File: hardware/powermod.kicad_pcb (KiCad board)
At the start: 4 copper layers, 65 x 40 mm, 77 parts, among them J1 USB_C_IN, J2 USB_C_OUT, J3 JST_PH_2, J4 STEMMA_QT, J5 SWD_HDR, Q1 AON7407, Q2 AON7407, Q3 BSS138, SW1 BUTTON, U1 BM8563, U2 PY32F003F18P6, U3 TPS63020DSJR, U4 TP4056, U5 XC6206P332MR, Y1 32.768kHz

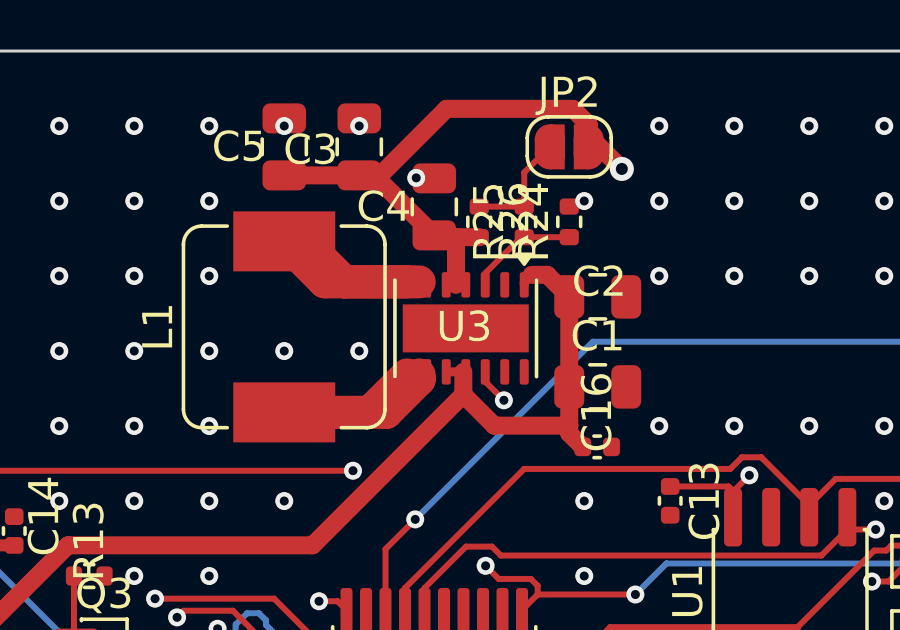
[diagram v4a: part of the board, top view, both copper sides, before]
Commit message: hardware: restore U3 EP plane-tie vias + silk-free gerbers
Validating user's U3 route tweaks (DRC 0, pad-diff 0, VOUT widened to 0.6mm)
surfaced that U3's exposed pad (TPS63020 PGND) had lost its plane-tie/thermal
vias in the re-routes - 0 vias in-pad, nearest GND via 3.6mm. Added 3 tented
GND vias in the EP (drill-safe spacing), DRC still 0. U4 EP already had 1.

Gerbers regenerated WITHOUT F.SilkS/B.SilkS -> fabricated board has no
silkscreen (removes the 127 cosmetic silk warnings from the fab output). Board
file keeps silk for reference; reversible.

Co-Authored-By: Claude Opus 4.8 <noreply@anthropic.com>
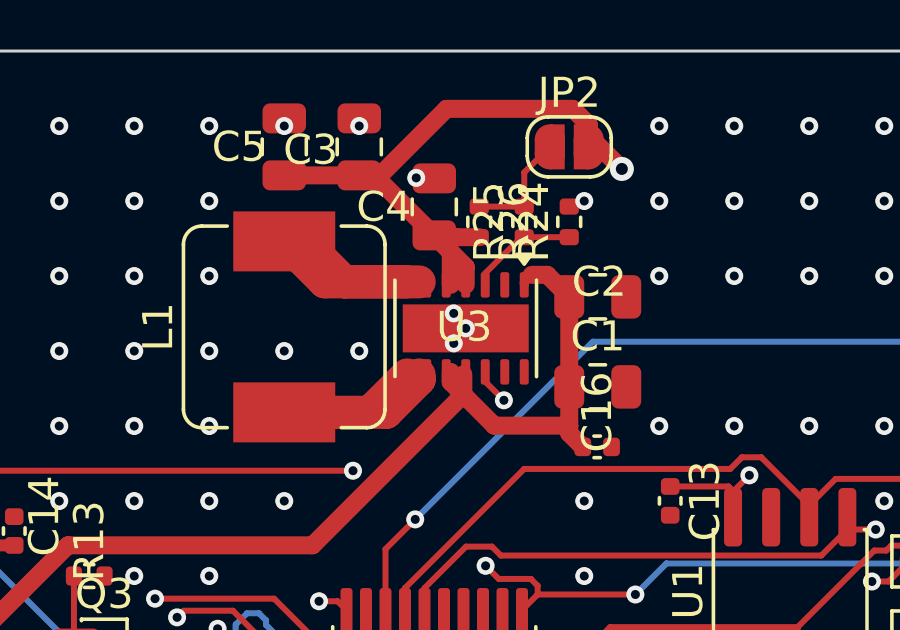
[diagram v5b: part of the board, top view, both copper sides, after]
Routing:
- net VOUT: track 75.1 -> 76.8 mm
- net GND: vias 157 -> 160
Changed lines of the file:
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@@
+	)
+	(via
+		(at 38.15 8.744999)
+		(size 0.6)
+		(drill 0.3)
+		(layers "F.Cu" "B.Cu")
+		(tenting
+			(front yes)
+			(back yes)
+		)
+		(net "GND")
 	)
 	(via
@@
 	)
 	(via
+		(at 38.55 9.245)
+		(size 0.6)
+		(drill 0.3)
+		(layers "F.Cu" "B.Cu")
+		(tenting
+			(front yes)
+			(back yes)
+		)
+		(net "GND")
+	)
+	(via
 		(at 52.5 5)
 		(size 0.6)
@@
 		(drill 0.3)
 		(layers "F.Cu" "B.Cu")
+		(net "GND")
+	)
+	(via
+		(at 38.15 9.744999)
+		(size 0.6)
+		(drill 0.3)
+		(layers "F.Cu" "B.Cu")
+		(tenting
+			(front yes)
+			(back yes)
+		)
 		(net "GND")
 	)
@@
 	)
 	(segment
+		(start 38.4687 11.4533)
+		(end 38.4687 10.7763)
+		(width 0.6)
+		(layer "F.Cu")
+		(net "VSYS")
+	)
+	(segment
 		(start 18.3998 24.3498)
 		(end 18.4 24.35)
@@
 		(start 18.7967 29.3967)
 		(end 19.7948 29.3967)
-		(width 0.6)
-		(layer "F.Cu")
-		(net "VSYS")
-	)
-	(segment
-		(start 37.9 10.695)
-		(end 38.4687 10.695)
-		(width 0.3004)
-		(layer "F.Cu")
-		(net "VSYS")
-	)
-	(segment
-		(start 38.4687 10.695)
-		(end 38.4687 11.4533)
 		(width 0.6)
 		(layer "F.Cu")
@@
 	)
 	(segment
+		(start 38.4687 11.4533)
+		(end 38.0498 11.0344)
+		(width 0.6)
+		(layer "F.Cu")
+		(net "VSYS")
+	)
+	(segment
 		(start 18.4 24.35)
 		(end 18.4 25)
@@
 	)
 	(segment
-		(start 38.4687 10.695)
-		(end 38.55 10.695)
-		(width 0.3004)
-		(layer "F.Cu")
-		(net "VSYS")
-	)
-	(segment
 		(start 27.275 28)
 		(end 27.4375 27.8375)
@@
 		(start 40.75 7.4602)
 		(end 41.2652 7.4602)
+		(width 0.6)
+		(layer "F.Cu")
+		(net "VSYS")
+	)
+	(segment
+		(start 38.0498 11.0344)
+		(end 38.0498 10.695)
 		(width 0.6)
 		(layer "F.Cu")
@@
 	)
 	(segment
+		(start 38.55 7.195)
+		(end 38.55 7.795)
+		(width 0.6)
+		(layer "F.Cu")
+		(net "VOUT")
+	)
+	(segment
 		(start 47.259332 27.0089)
 		(end 48.6093 27.0089)
@@
 	)
 	(segment
+		(start 38.0498 6.6948)
+		(end 38.0498 7.795)
+		(width 0.6)
+		(layer "F.Cu")
+		(net "VOUT")
+	)
+	(segment
 		(start 42.1183 1.9279)
 		(end 42.65 2.4596)
@@
 	)
 	(segment
-		(start 38.225 7.795)
-		(end 37.9 7.795)
-		(width 0.3004)
-		(layer "F.Cu")
-		(net "VOUT")
-	)
-	(segment
 		(start 51.7301 27.0089)
 		(end 52.52 27.7988)
@@
 	)
 	(segment
-		(start 38.55 7.795)
-		(end 38.225 7.795)
-		(width 0.3004)
-		(layer "F.Cu")
-		(net "VOUT")
-	)
-	(segment
 		(start 37.56 6.205)
 		(end 37.5 6.145)
@@
 	)
 	(segment
+		(start 37.5 6.145)
+		(end 38.55 7.195)
+		(width 0.6)
+		(layer "F.Cu")
+		(net "VOUT")
+	)
+	(segment
 		(start 35.0349 4.1799)
 		(end 35 4.145)
@@
 	)
 	(segment
-		(start 38.225 7.795)
-		(end 38.225 6.205)
-		(width 0.6)
-		(layer "F.Cu")
-		(net "VOUT")
-	)
-	(segment
 		(start 35.6566 4.1799)
 		(end 35.0349 4.1799)
 		(width 0.6)
 		(layer "F.Cu")
+		(net "VOUT")
+	)
+	(segment
+		(start 37.5 6.145)
+		(end 38.0498 6.6948)
+		(width 0.6)
+		(layer "F.Cu")

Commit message: hardware: FIX USB-C CC pins on wrong pads (mirrored footprint) [reroute pending]
CRITICAL: the local merged-pad USB-C footprint's inner-pin NAMES are mirrored
vs the real C165948 land pattern (verified pad-for-pad against the LCSC model).
GND/VBUS sit on symmetric positions (were fine), but CC1/CC2 were on the wrong
pads - the 5.1k pulldowns landed on the part's NC pins (A8/B8) and the real CC
pins (A5/B5 positions) were unconnected. A USB-C source would never enable VBUS
= board dead on USB power (exactly the spec's warned failure).

Fix: CC1/CC2 moved to pads A8/B8 (the real CC pin positions) on J1+J2, in
netlist.py and the board; A5/B5 -> NC. Stripped the 12 old CC track segments.
pad-diff 226/226 -> board matches corrected netlist. 4 CC connections now
unrouted (fine-pitch USB-C escape = interactive routing, like the other USB-C
pins) - hand-route next.

Co-Authored-By: Claude Opus 4.8 <noreply@anthropic.com>
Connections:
- J1 pad A5: CC1_IN -> (no net)
- J1 pad A8: (no net) -> CC1_IN
- J1 pad B5: CC2_IN -> (no net)
- J1 pad B8: (no net) -> CC2_IN
- J2 pad A5: CC1_OUT -> (no net)
- J2 pad A8: (no net) -> CC1_OUT
- J2 pad B5: CC2_OUT -> (no net)
- J2 pad B8: (no net) -> CC2_OUT
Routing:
- net CC1_IN: track 11.0 -> 0.00 mm
- net CC2_IN: track 6.83 -> 0.00 mm
- net CC1_OUT: track 3.53 -> 0.00 mm
- net CC2_OUT: track 3.11 -> 0.00 mm
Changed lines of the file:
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@@
 			(layers "F.Cu" "F.Mask" "F.Paste")
 			(roundrect_rratio 0.25)
-			(net "CC1_IN")
 		)
 		(pad "A6" smd roundrect
@@
 			(layers "F.Cu" "F.Mask" "F.Paste")
 			(roundrect_rratio 0.25)
+			(net "CC1_IN")
 		)
 		(pad "A9" smd roundrect
@@
 			(layers "F.Cu" "F.Mask" "F.Paste")
 			(roundrect_rratio 0.25)
-			(net "CC2_IN")
 		)
 		(pad "B6" smd roundrect
@@
 			(layers "F.Cu" "F.Mask" "F.Paste")
 			(roundrect_rratio 0.25)
+			(net "CC2_IN")
 		)
 		(pad "SH" thru_hole oval
@@
 			(layers "F.Cu" "F.Mask" "F.Paste")
 			(roundrect_rratio 0.25)
-			(net "CC1_OUT")
 		)
 		(pad "A6" smd roundrect
@@
 			(layers "F.Cu" "F.Mask" "F.Paste")
 			(roundrect_rratio 0.25)
+			(net "CC1_OUT")
 		)
 		(pad "A9" smd roundrect
@@
 			(layers "F.Cu" "F.Mask" "F.Paste")
 			(roundrect_rratio 0.25)
-			(net "CC2_OUT")
 		)
 		(pad "B6" smd roundrect
@@
 			(layers "F.Cu" "F.Mask" "F.Paste")
 			(roundrect_rratio 0.25)
+			(net "CC2_OUT")
 		)
 		(pad "SH" thru_hole oval
@@
 	)
 	(segment
-		(start 7.9452 13.75)
-		(end 8.945 13.75)
-		(width 0.2)
-		(layer "F.Cu")
-		(net "CC1_IN")
-	)
-	(segment
-		(start 2.99 21.5)
-		(end 2.7364 21.2464)
-		(width 0.2)
-		(layer "F.Cu")
-		(net "CC1_IN")
-	)
-	(segment
-		(start 2.7364 21.2464)
-		(end 2.7364 18.9588)
-		(width 0.2)
-		(layer "F.Cu")
-		(net "CC1_IN")
-	)
-	(segment
-		(start 2.7364 18.9588)
-		(end 7.9452 13.75)
-		(width 0.2)
-		(layer "F.Cu")
-		(net "CC1_IN")
-	)
-	(segment
-		(start 6.5971 21.1071)
-		(end 6.5971 17.483)
-		(width 0.2)
-		(layer "F.Cu")
-		(net "CC2_IN")
-	)
-	(segment
-		(start 6.99 21.5)
-		(end 6.5971 21.1071)
-		(width 0.2)
-		(layer "F.Cu")
-		(net "CC2_IN")
-	)
-	(segment
-		(start 7.3301 16.75)
-		(end 8.945 16.75)
-		(width 0.2)
-		(layer "F.Cu")
-		(net "CC2_IN")
-	)
-	(segment
-		(start 6.5971 17.483)
-		(end 7.3301 16.75)
-		(width 0.2)
-		(layer "F.Cu")
-		(net "CC2_IN")
-	)
-	(segment
 		(start 34.3719 26.5922)
 		(end 32.1034 26.5922)
@@
 	)
 	(segment
-		(start 48.75 29.26)
-		(end 48.75 31.005)
-		(width 0.2)
-		(layer "F.Cu")
-		(net "CC1_OUT")
-	)
-	(segment
-		(start 47.49 28)
-		(end 48.75 29.26)
-		(width 0.2)
-		(layer "F.Cu")
-		(net "CC1_OUT")
-	)
-	(segment
 		(start 12.5988 15.115)
 		(end 11.6514 14.1676)
@@
 	)
 	(segment
-		(start 51.75 31.005)
-		(end 51.75 28.25)
-		(width 0.2)
-		(layer "F.Cu")
-		(net "CC2_OUT")
-	)
-	(segment
-		(start 51.75 28.25)
-		(end 51.5 28)
-		(width 0.2)
-		(layer "F.Cu")
-		(net "CC2_OUT")
-	)
-	(segment

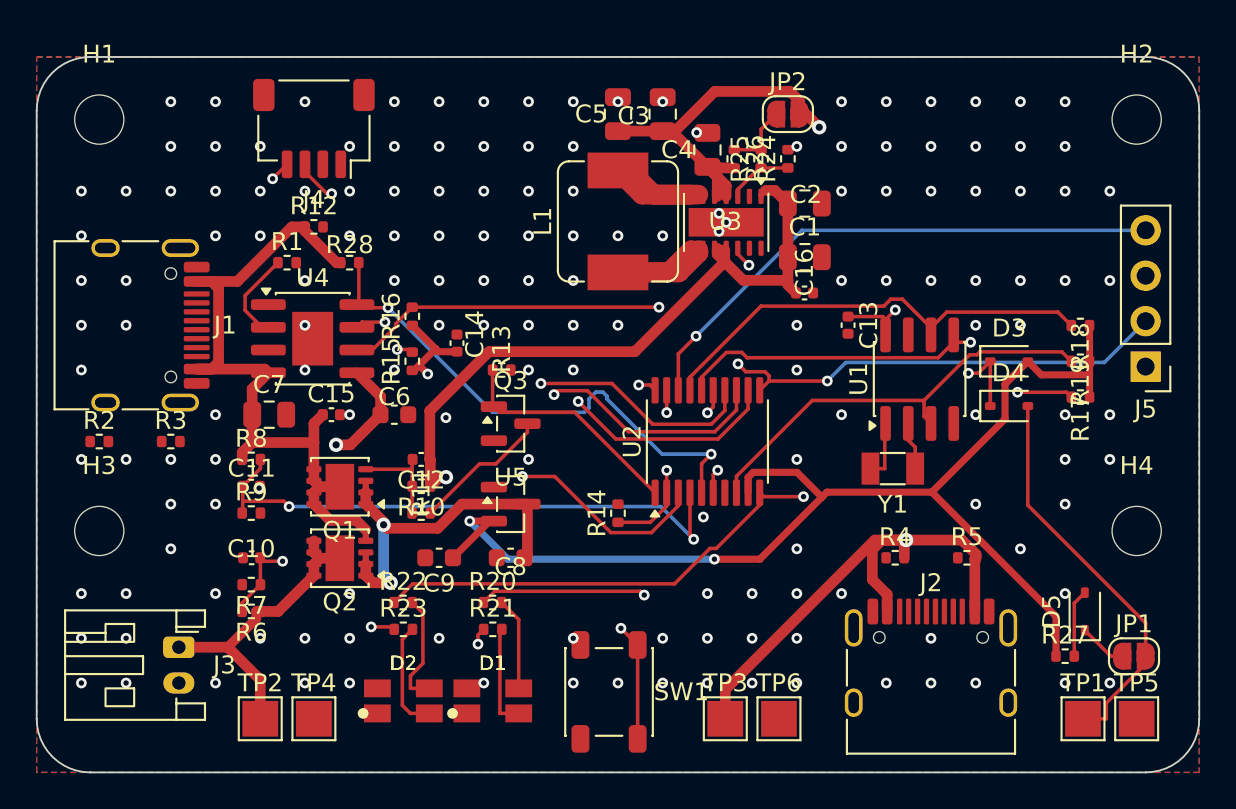
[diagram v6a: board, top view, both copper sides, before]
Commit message: hardware: full reroute after CC-resistor relocation; CC pins now routed
User relocated R2-R5 (the CC resistors) to suit the corrected CC pad positions.
Full Freerouting reroute (121->8). Freerouting routed all four CC pins (A8/B8,
0.3mm) this time - the USB-C CC fix is now fully wired. Re-added 4 tented GND
vias to the U3 EP (stripped in the reroute). 384 tracks, 183 vias, pad-diff
226/226.

Remaining (as expected from a full reroute): 4 USB-C large-pad escapes
(VBUS->J1 A4/A9, VOUT->J2 A4/A9) to hand-route, and the L1N/L2 switch node
reverted to trunk+neck (the 4 track_width flags are back) - re-widen to
uniform 1.1mm.

Co-Authored-By: Claude Opus 4.8 <noreply@anthropic.com>
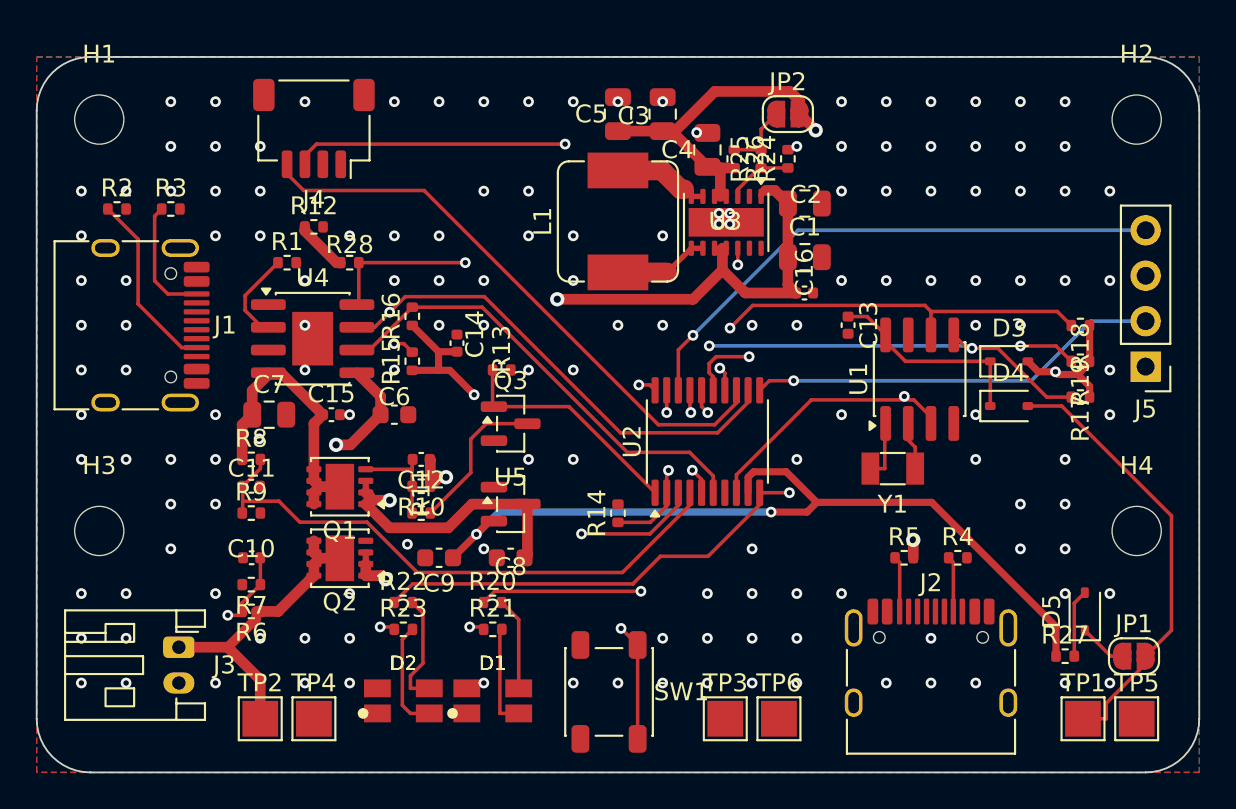
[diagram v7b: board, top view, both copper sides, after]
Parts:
- moved R2 13.0 mm to (4.49, 8.50)
- moved R3 13.0 mm to (7.50, 8.50)
- moved R5 3.51 mm to (48.5, 28.0)
- moved R4 3.50 mm to (51.5, 28.0)
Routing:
- net VOUT: track 76.8 -> 46.0 mm
- net VBUS: track 40.9 -> 19.0 mm
- net CHG_STDBY: track 39.1 -> 25.8 mm, vias 2 -> 0
- net 3V3: track 82.4 -> 93.4 mm, vias 3 -> 4
- net CC1_IN: track 0.00 -> 10.3 mm
- net CC2_IN: track 0.00 -> 6.83 mm
- net LED_PWR_B: track 26.1 -> 32.6 mm
- net L1N: track 9.72 -> 5.31 mm
- net L2: track 9.72 -> 5.35 mm
- net RTC_SCL: track 25.6 -> 29.9 mm, vias 0 -> 2
- net RTC_SDA: track 24.2 -> 27.9 mm, vias 2 -> 3
- net LED_BAT_B: track 54.0 -> 57.2 mm, vias 3 -> 2
- net CC2_OUT: track 0.00 -> 3.11 mm
- net CC1_OUT: track 0.00 -> 3.11 mm
- net CHG_CE: track 29.3 -> 31.8 mm
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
